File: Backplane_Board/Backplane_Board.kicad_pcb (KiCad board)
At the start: 2 copper layers, 156 parts, among them J1 XT60, J10 Conn_01x02_Pin, J11 Conn_01x02_Pin, J12 Conn_01x02_Pin, J13 Conn_01x02_Pin, J14 Conn_01x02_Pin, J15 Conn_01x02_Pin, J16 Conn_01x02_Pin, J17 Conn_01x02_Pin, J18 Conn_01x02_Pin, J19 Conn_01x02_Pin, J2 XT60, J20 Conn_01x02_Pin, J21 Conn_01x02_Pin, J22 Conn_01x02_Pin, J23 Conn_01x02_Pin, J24 Conn_01x02_Pin, J25 Conn_01x03_Pin, J26 Conn_01x03_Pin, J27 Conn_01x03_Pin, J28 BM03B-SRSS-TB, J29 Conn_01x04, J3 Conn_01x02_Pin, J30 Conn_01x05_Socket, J31 BM03B-SRSS-TB, J32 Conn_01x03_Pin, J33 Conn_01x03_Pin, J34 Conn_01x03_Pin, J4 Conn_01x07_Female, J5 Conn_01x02_Pin, J6 Conn_01x02_Pin, J7 Conn_01x02_Pin, J8 Conn_01x02_Pin, J9 Conn_01x02_Pin, Q1 FDMS86163P, Q2 FDMS86163P, Q3 SI7615ADN-T1-GE3, Q4 ZXMN3A14F, Q5 ZXMN3A14F, Q6 ZXMN3A14F, Q7 ZXMN3A14F, Q8 ZXMN3A14F, Q9 ZXMN3A14F, SW1 SW_DPST_x2, U1 ZXTR2005ZQ-13, U2 PINA740AIREMR, U3 PKJ7213WPI, U4 PKJ7213WPI, U5 PKU3511SPI, U6 Pico

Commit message: derat nest ifcation
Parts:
- removed C27, C28: 2.2uF+/35V+, Capacitor_SMD:C_0805_2012Metric
- added C10: 22uF, Capacitor_SMD:C_1206_3216Metric_Pad1.33x1.80mm_HandSolder, F.Cu at (108.8, 116.3)
- added C11: 22uF, Capacitor_SMD:C_1206_3216Metric_Pad1.33x1.80mm_HandSolder, F.Cu at (108.8, 119.7)
- added C12: 22uF, Capacitor_SMD:C_1206_3216Metric_Pad1.33x1.80mm_HandSolder, F.Cu at (108.8, 123.0)
- added C13: 680u, Capacitor_THT:CP_Radial_D13.0mm_P5.00mm, F.Cu at (119.1, 74.3)
- added C16: 22uF, Capacitor_SMD:C_1206_3216Metric_Pad1.33x1.80mm_HandSolder, F.Cu at (87.2, 60.6)
- added C17: 22uF, Capacitor_SMD:C_1206_3216Metric_Pad1.33x1.80mm_HandSolder, F.Cu at (90.5, 60.6)
- added C18: 22uF, Capacitor_SMD:C_1206_3216Metric_Pad1.33x1.80mm_HandSolder, F.Cu at (93.8, 60.6)
- added C19: 330 uF, Capacitor_SMD:CP_Elec_6.3x7.7, F.Cu at (131.5, 31.9)
- added C20: 330 uF, Capacitor_SMD:CP_Elec_6.3x7.7, F.Cu at (132.0, 45.9)
- added C21: 2.2uF+/35V+, Capacitor_SMD:C_0805_2012Metric, F.Cu at (182.4, 109.8)
- added C22: 2.2uF+/35V+, Capacitor_SMD:C_0805_2012Metric, F.Cu at (187.8, 151.3)
- added C9: 22uF, Capacitor_SMD:C_1206_3216Metric_Pad1.33x1.80mm_HandSolder, F.Cu at (108.8, 113.0)
- added J35: Connector_PinHeader_2.54mm:PinHeader_1x03_P2.54mm_Vertical, Connector_PinHeader_2.54mm:PinHeader_1x03_P2.54mm_Vertical, F.Cu at (195.8, 39.8)
- added J36: Conn_01x03_Pin, Connector_PinHeader_2.54mm:PinHeader_1x03_P2.54mm_Vertical, F.Cu at (187.8, 39.8)
- added J37: Conn_01x02, Connector_Molex:Molex_Micro-Latch_53253-0270_1x02_P2.00mm_Vertical, F.Cu at (197.5, 110.1)
- added J38: Conn_01x02, Connector_Molex:Molex_Micro-Latch_53253-0270_1x02_P2.00mm_Vertical, F.Cu at (204.3, 145.3)
- added J39: Conn_01x02, Connector_Molex:Molex_Micro-Latch_53253-0270_1x02_P2.00mm_Vertical, F.Cu at (203.9, 127.5)
- added J40: Conn_01x02, Connector_Molex:Molex_Micro-Latch_53253-0270_1x02_P2.00mm_Vertical, F.Cu at (256.3, 46.4)
- added J41: Conn_01x02, Connector_Molex:Molex_Micro-Latch_53253-0270_1x02_P2.00mm_Vertical, F.Cu at (273.2, 46.6)
- added J42: Conn_01x02, Connector_Molex:Molex_Micro-Latch_53253-0270_1x02_P2.00mm_Vertical, F.Cu at (240.6, 46.0)
- added R46: 1k, Resistor_SMD:R_0805_2012Metric_Pad1.20x1.40mm_HandSolder, F.Cu at (149.8, 41.5)
- C15: value 680u -> 22uF; footprint Capacitor_THT:CP_Radial_D13.0mm_P5.00mm -> Capacitor_SMD:C_1206_3216Metric_Pad1.33x1.80mm_HandSolder
- J1, J2: footprint Connector_AMASS:AMASS_XT30U-F_1x02_P5.0mm_Vertical -> Connector_Wire:SolderWire-2sqmm_1x02_P7.8mm_D2mm_OD3.9mm
- J11, J12, J13, J14, J15, J16: footprint TerminalBlock:TerminalBlock_Xinya_XY308-2.54-2P_1x02_P2.54mm_Horizontal -> Connector_AMASS:AMASS_XT30U-M_1x02_P5.0mm_Vertical
- J19, J6, J7, J8: footprint Connector_AMASS:AMASS_XT30U-M_1x02_P5.0mm_Vertical -> TerminalBlock_4Ucon:TerminalBlock_4Ucon_1x02_P3.50mm_Horizontal
- J22, J23: footprint TerminalBlock_4Ucon:TerminalBlock_4Ucon_1x02_P3.50mm_Horizontal -> Connector_AMASS:AMASS_XT30U-M_1x02_P5.0mm_Vertical
- J24: footprint TestPoint:TestPoint_2Pads_Pitch2.54mm_Drill0.8mm -> Connector_AMASS:AMASS_XT30U-M_1x02_P5.0mm_Vertical
- J25: value Conn_01x03_Pin -> Conn_01x02_Pin; footprint TerminalBlock:TerminalBlock_Xinya_XY308-2.54-3P_1x03_P2.54mm_Horizontal -> Connector_AMASS:AMASS_XT30U-M_1x02_P5.0mm_Vertical
- J26: value Conn_01x03_Pin -> Conn_01x02_Pin; footprint TerminalBlock:TerminalBlock_Xinya_XY308-2.54-3P_1x03_P2.54mm_Horizontal -> TestPoint:TestPoint_2Pads_Pitch2.54mm_Drill0.8mm
- J27: footprint TerminalBlock:TerminalBlock_Xinya_XY308-2.54-3P_1x03_P2.54mm_Horizontal -> Connector_PinHeader_2.54mm:PinHeader_1x03_P2.54mm_Vertical
- J28: value BM03B-SRSS-TB -> Conn_01x03_Pin; footprint Connector_JST:JST_SH_BM03B-SRSS-TB_1x03-1MP_P1.00mm_Vertical -> Connector_PinHeader_2.54mm:PinHeader_1x03_P2.54mm_Vertical
- J29: value Conn_01x04 -> Conn_01x03_Pin; footprint Connector_PinSocket_1.00mm:PinSocket_1x04_P1.00mm_Vertical -> Connector_PinHeader_2.54mm:PinHeader_1x03_P2.54mm_Vertical
- J30: value Conn_01x05_Socket -> BM03B-SRSS-TB; footprint Connector_PinHeader_1.00mm:PinHeader_1x05_P1.00mm_Vertical -> Connector_JST:JST_SH_BM03B-SRSS-TB_1x03-1MP_P1.00mm_Vertical
- J31: value BM03B-SRSS-TB -> Conn_01x04; footprint Connector_JST:JST_SH_BM03B-SRSS-TB_1x03-1MP_P1.00mm_Vertical -> Connector_Molex:Molex_PicoBlade_53047-0410_1x04_P1.25mm_Vertical
- J32: value Conn_01x03_Pin -> Conn_01x05_Socket; footprint TerminalBlock:TerminalBlock_Xinya_XY308-2.54-3P_1x03_P2.54mm_Horizontal -> Connector_PinSocket_2.54mm:PinSocket_1x05_P2.54mm_Vertical
- J33: value Conn_01x03_Pin -> BM03B-SRSS-TB; footprint TerminalBlock:TerminalBlock_Xinya_XY308-2.54-3P_1x03_P2.54mm_Horizontal -> Connector_JST:JST_SH_BM03B-SRSS-TB_1x03-1MP_P1.00mm_Vertical
- J34: value Conn_01x03_Pin -> Connector_PinHeader_2.54mm:PinHeader_1x03_P2.54mm_Vertical; footprint TerminalBlock:TerminalBlock_Xinya_XY308-2.54-3P_1x03_P2.54mm_Horizontal -> Connector_PinHeader_2.54mm:PinHeader_1x03_P2.54mm_Vertical
- JP5: value Jumper_2_Open -> SolderJumper_2_Bridged; footprint Connector_AMASS:AMASS_XT60-F_1x02_P7.20mm_Vertical -> Jumper:SolderJumper-2_P1.3mm_Bridged_RoundedPad1.0x1.5mm
- R1: value 2k -> 8.8k
- R13, R2, R20, R23, R24, R3, R6: footprint Resistor_SMD:R_1206_3216Metric_Pad1.30x1.75mm_HandSolder -> Resistor_SMD:R_0805_2012Metric_Pad1.20x1.40mm_HandSolder
- R25, R26, R27: footprint Inductor_SMD:L_1206_3216Metric -> Resistor_SMD:R_0805_2012Metric_Pad1.20x1.40mm_HandSolder
- U5: moved to B.Cu
- moved D22 599.1 mm to (280.7, 47.3), turned to 90 degrees
- moved Q8 595.5 mm to (274.3, 59.1)
- moved D27 593.3 mm to (281.1, 52.7)
- moved F11 586.5 mm to (269.7, 51.9), turned to 90 degrees
- moved R38 585.0 mm to (279.8, 57.1)
- moved F10 580.5 mm to (262.8, 46.3), turned to 90 degrees
- moved R44 579.1 mm to (279.7, 60.6)
- moved R42 578.4 mm to (269.8, 56.6)
- moved Q7 577.8 mm to (257.1, 58.6)
- moved D26 574.6 mm to (262.4, 52.8)
- moved D24 573.5 mm to (274.2, 52.8)
- moved R41 570.9 mm to (263.5, 59.0)
- moved D20 569.6 mm to (252.0, 51.7)
- moved Q9 565.9 mm to (242.1, 58.5)
- moved C25 563.5 mm to (268.6, 44.6), turned to 90 degrees
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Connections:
- C15 pad 1: 12V_ESC -> GND
- C15 pad 2: GND -> Net-(C15-Pad2)
- C23 pad 1: Net-(D14-K) -> Net-(D16-K)
- C24 pad 1: Net-(D15-K) -> Net-(D21-K)
- C25 pad 1: Net-(D16-K) -> Net-(D24-K)
- C26 pad 1: Net-(D21-K) -> Net-(D25-K)
- D4 pad 2: Net-(D4-A) -> +12V
- F1 pad 2: Net-(J25-Pin_2) -> Net-(J27-Pin_2)
- F2 pad 2: Net-(J26-Pin_2) -> Net-(J28-Pin_2)
- F3 pad 2: Net-(J27-Pin_2) -> Net-(J29-Pin_2)
- F4 pad 2: Net-(J32-Pin_2) -> Net-(J34-Pin_2)
- F5 pad 2: Net-(J33-Pin_2) -> Net-(J35-Pin_2)
- F6 pad 2: Net-(J34-Pin_2) -> Net-(J36-Pin_2)
- J11 pad 2: +5V -> 12V_ESC
- J12 pad 2: +5V -> 12V_ESC
- J13 pad 2: +5V -> 12V_ESC
- J14 pad 2: +5V -> 12V_ESC
- J15 pad 2: +5V -> 12V_ESC
- J16 pad 2: +5V -> 12V_ESC
- J19 pad 2: 12V_ESC -> +5V
- J20 pad 2: +12V -> +5V
- J21 pad 2: +12V -> +5V
- J24 pad 1: 60V -> GND
- J24 pad 2: GND -> +12V
- J25 pad 2: Net-(J25-Pin_2) -> +12V
- J26 pad 1: GND -> 60V
- J26 pad 2: Net-(J26-Pin_2) -> GND
- J28 pad 1: UART(RX) -> GND
- J28 pad 2: GND -> Net-(J28-Pin_2)
- J28 pad 3: UART(TX) -> SERVO0
- J29 pad 2: +3.3V -> Net-(J29-Pin_2)
- J29 pad 3: SDA -> SERVO0
- J30 pad 1: +3.3V -> UART(RX)
- J30 pad 2: RUN -> GND
- J30 pad 3: SDA -> UART(TX)
- J31 pad 1: SWDIO -> GND
- J31 pad 2: GND -> +3.3V
- J31 pad 3: SWCLK -> SDA
- J32 pad 1: GND -> +3.3V
- J32 pad 2: Net-(J32-Pin_2) -> RUN
- J32 pad 3: SERVO0 -> SDA
- J33 pad 1: GND -> SWDIO
- J33 pad 2: Net-(J33-Pin_2) -> GND
- J33 pad 3: SERVO0 -> SWCLK
- J6 pad 2: 12V_ESC -> +5V
- J7 pad 2: 12V_ESC -> +5V
- J8 pad 2: 12V_ESC -> +5V
- JP5 pad 1: Net-(D4-A) -> esc_status
- JP5 pad 2: +12V -> KillSW
- R12 pad 2: Net-(D4-A) -> +12V
- R14 pad 2: Net-(C16-Pad2) (its old number) -> Net-(C15-Pad2)
- R27 pad 1: Net-(U6-GPIO16) -> Net-(D10-A)
- R27 pad 2: Net-(D10-A) -> Net-(U6-GPIO16)
- U4 pad 8: Net-(D4-A) -> +12V
- U4 pad 9: Net-(D4-A) -> +12V
- U6 pad 26: unconnected-(U6-GPIO20-Pad26)_1 -> esc_status
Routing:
- net GND: track 0.00 -> 20.8 mm, vias 0 -> 2
- net Net-(D14-K): track 0.00 -> 20.0 mm
- net Net-(D14-A): track 0.00 -> 14.7 mm
- net Net-(D17-A): track 0.00 -> 9.73 mm
- net SW2: track 0.00 -> 9.23 mm
- net Net-(D11-A): track 0.00 -> 6.74 mm
- net +12V: track 0.00 -> 2.46 mm, vias 0 -> 1
- added copper zone on B.Cu, net GND
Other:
- board outline added: 179.7 x 127.9 mm

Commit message: got the power input shut layout done ish
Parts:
- J1, J2: footprint Connector_Wire:SolderWire-2sqmm_1x02_P7.8mm_D2mm_OD3.9mm -> Connector_Wire:SolderWire-0.127sqmm_1x02_P3.7mm_D0.48mm_OD1mm
- JP1, JP2, JP3, JP4: moved to B.Cu
- moved J38 120.0 mm to (181.0, 27.7), turned to 0 degrees
- moved J7 118.3 mm to (193.7, 144.5), turned to 0 degrees
- moved D12 117.8 mm to (180.2, 32.1), turned to -90 degrees
- moved R29 117.2 mm to (179.5, 38.6), turned to 180 degrees
- moved J6 116.9 mm to (201.7, 136.9), turned to 90 degrees
- moved J19 116.3 mm to (203.0, 144.5), turned to 0 degrees
- moved D18 113.7 mm to (182.0, 32.1), turned to -90 degrees
- moved D15 112.7 mm to (181.6, 34.8), turned to 0 degrees
- moved D22 112.6 mm to (179.6, 96.7)
- moved D27 112.4 mm to (177.7, 96.8), turned to 90 degrees
- moved D26 109.6 mm to (161.9, 96.6), turned to 90 degrees
- moved J41 109.1 mm to (178.8, 101.2), turned to 180 degrees
- moved C22 108.8 mm to (180.9, 42.8), turned to -90 degrees
- moved Q5 108.2 mm to (184.3, 38.4)
- moved J40 108.1 mm to (163.0, 101.0), turned to 180 degrees
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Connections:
- net Net-(J1-Pin_2) renamed PWR_IN
- F7 pad 2: +12V -> 12V_ESC
- F8 pad 2: +12V -> 12V_ESC
- F9 pad 2: +12V -> 12V_ESC
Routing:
- net GND: track 20.8 -> 157.4 mm, vias 2 -> 38
- net Net-(D1-A): track 0.00 -> 21.8 mm, vias 0 -> 2
- net Net-(D24-K): track 0.00 -> 20.0 mm
- net Net-(D21-K): track 0.00 -> 20.0 mm
- net Net-(D25-K): track 0.00 -> 20.0 mm
- net Net-(D16-K): track 0.00 -> 20.0 mm
- net Net-(D15-K): track 0.00 -> 20.0 mm
- net 12V_ESC: track 0.00 -> 19.0 mm, vias 0 -> 3
- net 60V: track 0.00 -> 16.7 mm, vias 0 -> 59
- net Net-(D25-A): track 0.00 -> 14.7 mm
- net Net-(D24-A): track 0.00 -> 14.7 mm
- net Net-(D16-A): track 0.00 -> 14.7 mm
- net Net-(D15-A): track 0.00 -> 14.7 mm
- net Net-(D21-A): track 0.00 -> 14.7 mm
- net A1: track 0.00 -> 11.9 mm, vias 0 -> 1
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- added copper zone on In2.Cu, net 12V_ESC
- added copper zone on F.Cu, net 60V
- added copper zone on In2.Cu, net 60V
- added copper zone on In1.Cu, net GND
- added copper zone on F.Cu, net PWR_IN
- added copper zone on F.Cu, net SHUNT+
- added copper zone on In2.Cu, net SHUNT+
- removed copper zone on B.Cu, net GND
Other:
- copper layers 2 -> 4

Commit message: layout save
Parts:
- moved D7 28.6 mm to (162.2, 115.5)
- moved R24 28.5 mm to (158.5, 115.5)
- moved D5 25.9 mm to (182.7, 143.8), turned to 0 degrees
- moved R20 20.0 mm to (178.5, 143.8), turned to 180 degrees
- moved R17 15.2 mm to (120.5, 114.0), turned to 180 degrees
- moved R16 12.5 mm to (120.5, 117.1), turned to 180 degrees
- moved C18 11.4 mm to (115.3, 114.0), turned to 0 degrees
- moved R14 11.2 mm to (120.5, 123.4), turned to 180 degrees
- moved R15 11.0 mm to (120.5, 120.2), turned to 180 degrees
- moved R46 8.34 mm to (201.5, 119.2), turned to 0 degrees
- moved C17 7.44 mm to (115.3, 116.9), turned to 0 degrees
- moved C15 4.54 mm to (115.3, 123.2), turned to 0 degrees
- moved C20 4.42 mm to (174.8, 137.2)
- moved C16 3.91 mm to (115.3, 120.2), turned to 0 degrees
- moved J34 3.85 mm to (197.5, 111.0), turned to 180 degrees
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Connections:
- C13 pad 1: 12V_ESC -> +12V
- C14 pad 1: 12V_ESC -> +12V
- R14 pad 1: 12V_ESC -> +12V
- R15 pad 1: 12V_ESC -> +12V
- R16 pad 1: 12V_ESC -> +12V
- R17 pad 1: 12V_ESC -> +12V
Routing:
- net +5V: track 7.37 -> 81.8 mm, vias 0 -> 35
- net GND: track 157.4 -> 190.6 mm, vias 38 -> 50
- net +12V: track 0.00 -> 18.0 mm, vias 0 -> 3
- net Net-(U4-V_adj): track 0.00 -> 7.80 mm
- net Net-(U5-TRIM): track 0.00 -> 7.75 mm
- net Net-(Q3-G): track 0.00 -> 5.00 mm
- net Net-(D6-K): track 0.00 -> 4.44 mm
- net Net-(J28-Pin_2): track 0.00 -> 4.13 mm
- net Net-(J34-Pin_2): track 0.00 -> 4.06 mm
- net Net-(J27-Pin_2): track 0.00 -> 4.06 mm
- net Net-(J29-Pin_2): track 0.00 -> 4.04 mm
- net Net-(J35-Pin_2): track 0.00 -> 4.03 mm
- net Net-(J36-Pin_2): track 0.00 -> 4.01 mm
- net Net-(C17-Pad2): track 0.00 -> 2.47 mm
- net Net-(D5-K): track 0.00 -> 2.43 mm
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- added copper zone on In2.Cu, net +12V
- added copper zone on F.Cu, net +5V
- added copper zone on In2.Cu, net +5V
- added copper zone on F.Cu, net 5V_KillSW
- added copper zone on In2.Cu, net 5V_KillSW

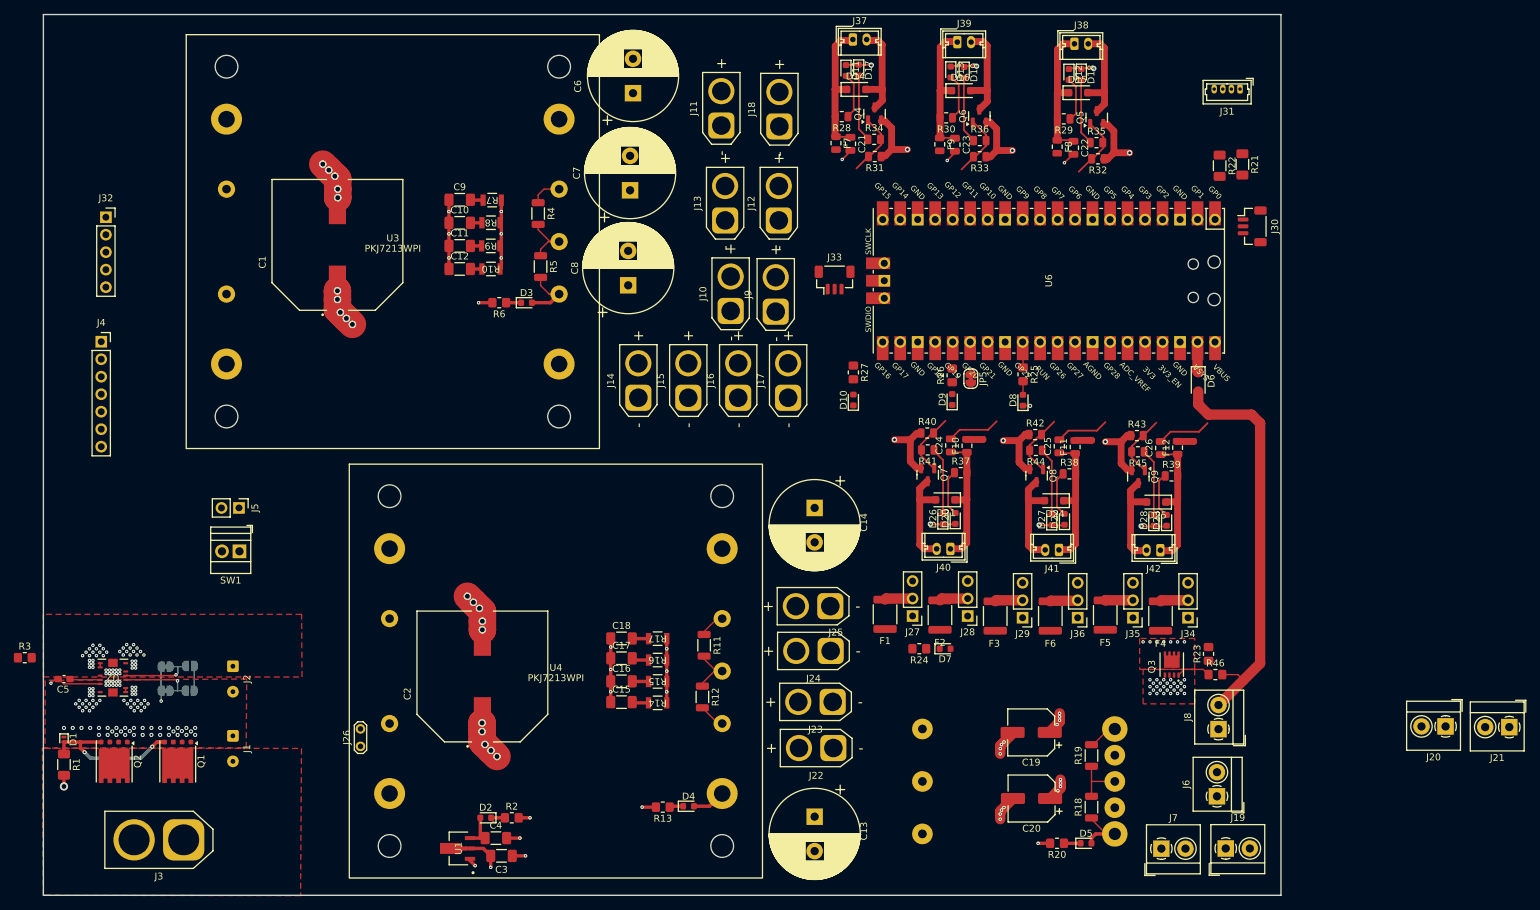
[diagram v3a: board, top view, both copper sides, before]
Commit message: rough layout compleat, 200+ drc errors to fix
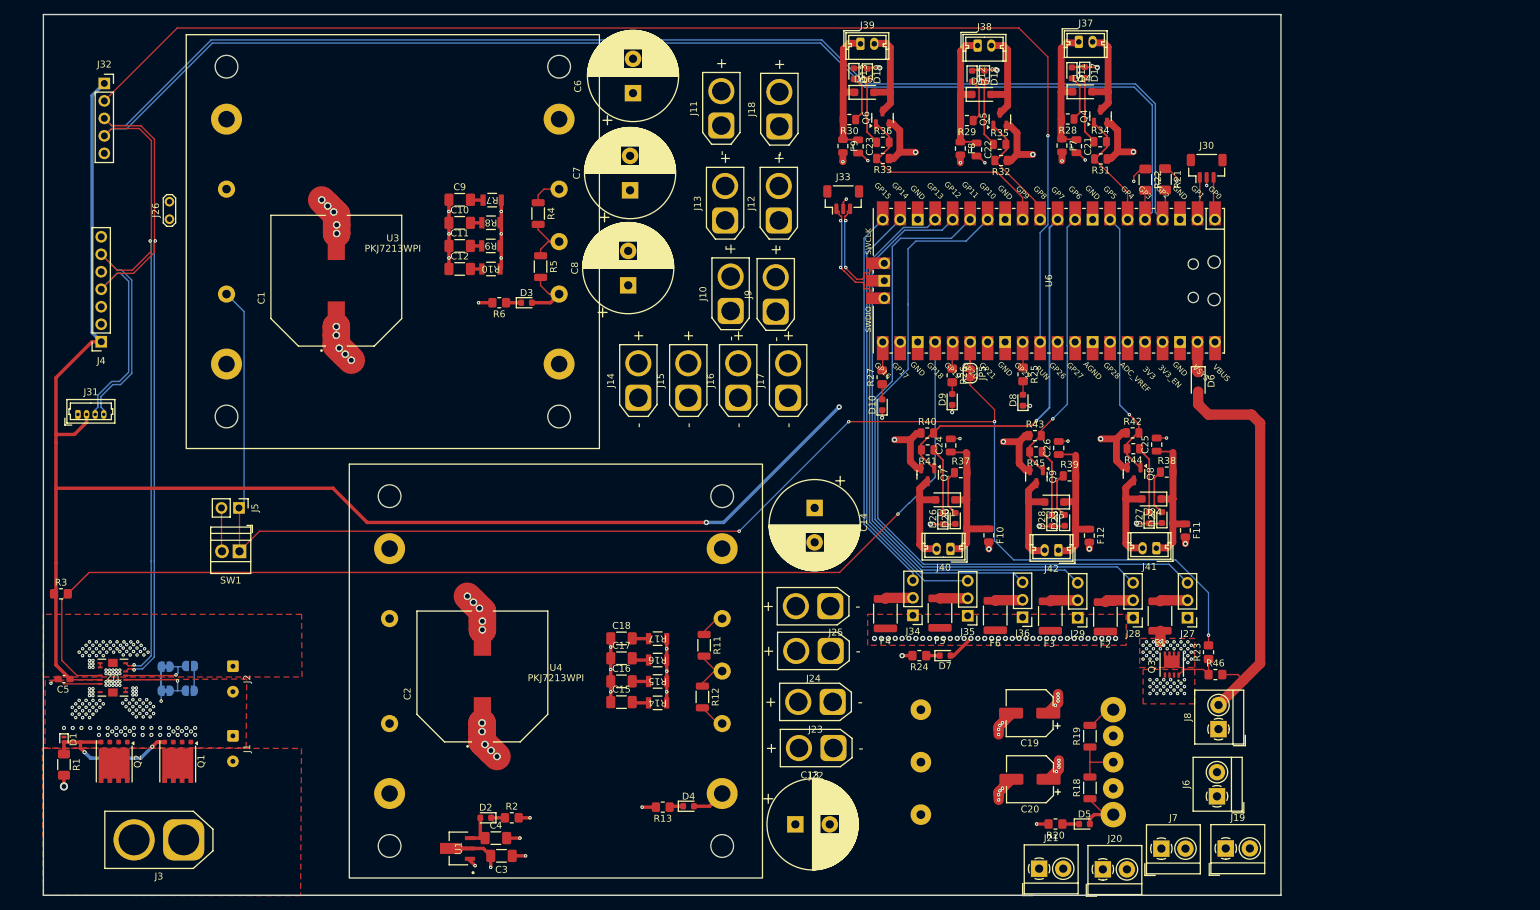
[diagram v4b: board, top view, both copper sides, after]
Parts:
- moved J31 175.2 mm to (36.3, 81.5), turned to 0 degrees
- moved J26 81.4 mm to (49.6, 53.1)
- moved J21 71.3 mm to (175.9, 147.4), turned to 0 degrees
- moved J20 53.9 mm to (185.2, 147.5), turned to 0 degrees
- moved F4 40.0 mm to (153.6, 110.4)
- moved J34 40.0 mm to (157.6, 110.7)
- moved F1 39.9 mm to (193.4, 110.8)
- moved J27 39.9 mm to (197.4, 111.0)
- moved D11 32.8 mm to (180.7, 31.9)
- moved D14 32.8 mm to (182.2, 34.6)
- moved D17 32.8 mm to (182.5, 31.8)
- moved J37 32.8 mm to (181.7, 27.4)
- moved R31 32.8 mm to (184.9, 44.4)
- moved R34 32.8 mm to (184.8, 41.9)
- moved C21 32.8 mm to (181.3, 42.5)
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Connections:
- net SWCLK renamed /BoardBoardConnections/DEBUG+
- net SWDIO renamed /BoardBoardConnections/DEBUG-
- F10 pad 2: +5V -> 5V_KillSW
- F11 pad 2: +5V -> 5V_KillSW
- F12 pad 2: +5V -> 5V_KillSW
- J28 pad 3: SERVO0 -> SERVO1
- J29 pad 3: SERVO0 -> SERVO2
- J31 pad 3: SDA -> I2C+
- J31 pad 4: SCL -> I2C-
- J32 pad 3: SDA -> I2C+
- J32 pad 4: SCL -> I2C-
- J34 pad 3: SERVO0 -> SERVO5
- J35 pad 3: SERVO0 -> SERVO4
- J36 pad 3: SERVO0 -> SERVO3
- J4 pad 4: SCL -> I2C+
- J4 pad 6: SDA -> I2C-
- R21 pad 2: SDA -> I2C+
- R22 pad 2: SCL -> I2C-
- U2 pad 5: SDA -> I2C+
- U2 pad 6: SCL -> I2C-
- U6 pad 4: SDA -> I2C+
- U6 pad 5: SCL -> I2C-
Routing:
- net I2C+: track 0.00 -> 312.0 mm, vias 0 -> 2
- net I2C-: track 0.00 -> 309.6 mm, vias 0 -> 2
- net +3.3V: track 4.46 -> 231.7 mm, vias 0 -> 4
- net KillSW: track 0.00 -> 224.2 mm, vias 0 -> 4
- net RUN: track 0.00 -> 185.0 mm, vias 0 -> 1
- net ALERT: track 0.00 -> 169.1 mm, vias 0 -> 1
- net SERVO0: track 0.00 -> 103.2 mm
- net SERVO1: track 0.00 -> 94.9 mm
- net SERVO2: track 0.00 -> 85.3 mm
- net SERVO3: track 0.00 -> 75.7 mm
- net SERVO4: track 0.00 -> 64.2 mm
- net SERVO5: track 0.00 -> 56.5 mm
- net SW5: track 9.23 -> 52.9 mm, vias 0 -> 1
- net SW4: track 9.23 -> 40.1 mm, vias 0 -> 1
- net SW3: track 9.23 -> 39.4 mm, vias 0 -> 1
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- added copper zone on In2.Cu, net +3.3V

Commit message: few drc errors left - must fix fet footprints
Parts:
- moved J26 56.3 mm to (71.6, 104.9)
- moved R22 28.4 mm to (207.0, 71.0), turned to 180 degrees
- moved R21 23.4 mm to (206.9, 67.0), turned to 180 degrees
- moved C18 14.9 mm to (113.7, 128.8)
- moved R17 14.7 mm to (119.7, 128.7)
- moved J20 13.4 mm to (171.8, 146.9)
- moved J21 13.4 mm to (162.5, 146.8)
- moved J19 13.2 mm to (190.0, 147.0)
- moved J7 12.9 mm to (181.0, 147.0)
- moved C17 8.37 mm to (113.7, 125.1)
- moved R16 7.90 mm to (119.7, 125.0)
- moved JP3 7.33 mm to (54.0, 116.2), turned to 0 degrees
- moved J32 7.05 mm to (35.6, 38.8)
- moved JP4 6.69 mm to (54.0, 113.5), turned to 0 degrees
- moved R14 5.97 mm to (119.7, 117.5)
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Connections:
- JP1 pad 2: SCL -> I2C-
- JP2 pad 2: SCL -> I2C-
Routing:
- net I2C-: track 309.6 -> 346.4 mm
- net I2C+: track 312.0 -> 333.5 mm
- net +3.3V: track 231.7 -> 221.3 mm, vias 4 -> 2
- net A0: track 11.0 -> 21.0 mm
- net RUN: track 185.0 -> 191.3 mm
- net A1: track 11.9 -> 17.7 mm
- net ALERT: track 169.1 -> 164.0 mm
- net KillSW: track 224.2 -> 219.6 mm, vias 4 -> 2
- net SERVO5: track 56.5 -> 60.6 mm
- net SCL: track 3.76 -> 0.00 mm
- net esc_status: track 3.88 -> 6.96 mm
- net Net-(U6-GPIO19): track 3.88 -> 6.87 mm
- net Net-(U6-GPIO22): track 3.85 -> 6.24 mm
- net SERVO4: track 64.2 -> 66.6 mm
- net Net-(U6-GPIO16): track 4.16 -> 6.31 mm
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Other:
- rule pad_to_mask_clearance: 0 -> 0.0508
